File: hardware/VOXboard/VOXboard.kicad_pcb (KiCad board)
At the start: 2 copper layers, 52 parts, among them J1 USB-C 2.0 16P, J8 8P8C_LED_Shielded_x4, Q1 2N7002, U1 OPA333, U3 OPA333, U4 STM32F411CEUx, U7 HT7533, Y1 12M

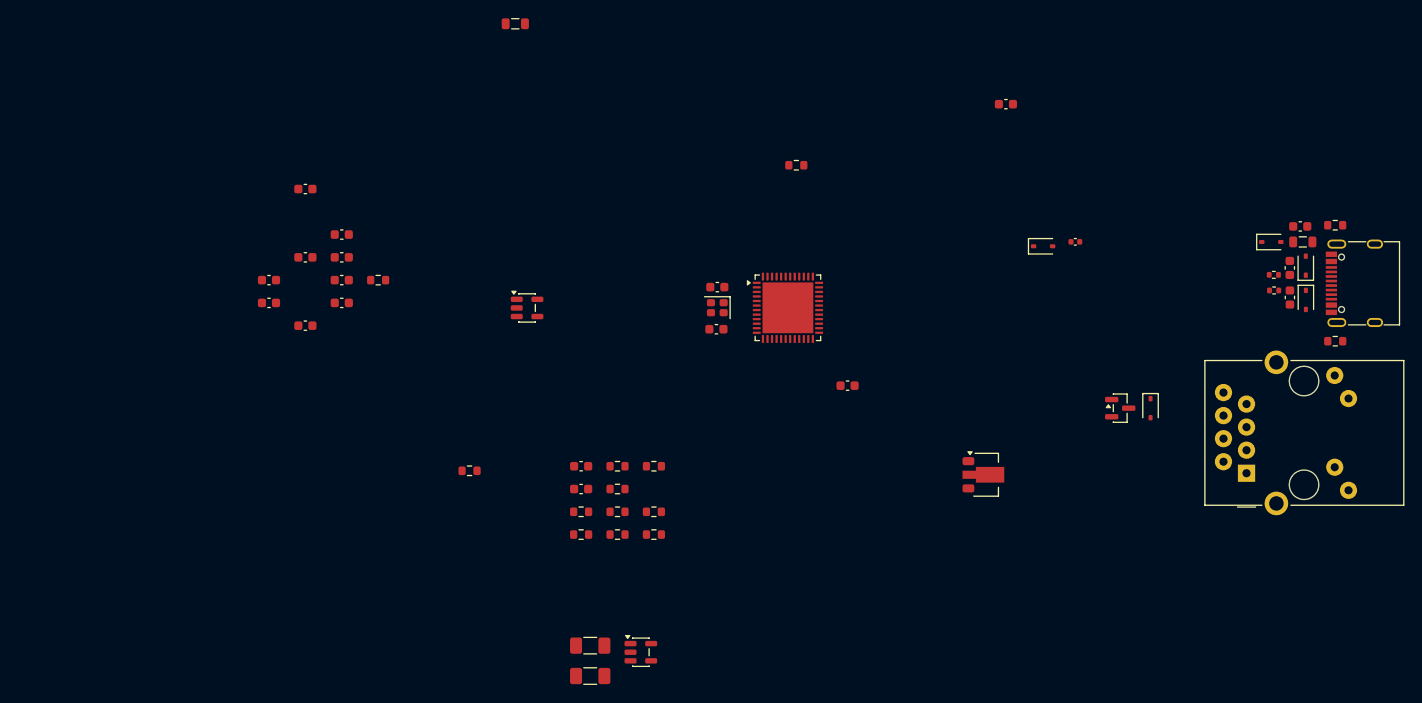
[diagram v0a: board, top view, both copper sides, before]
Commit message: Worked on OpAmp design in uSimmics.  Updated schematic.
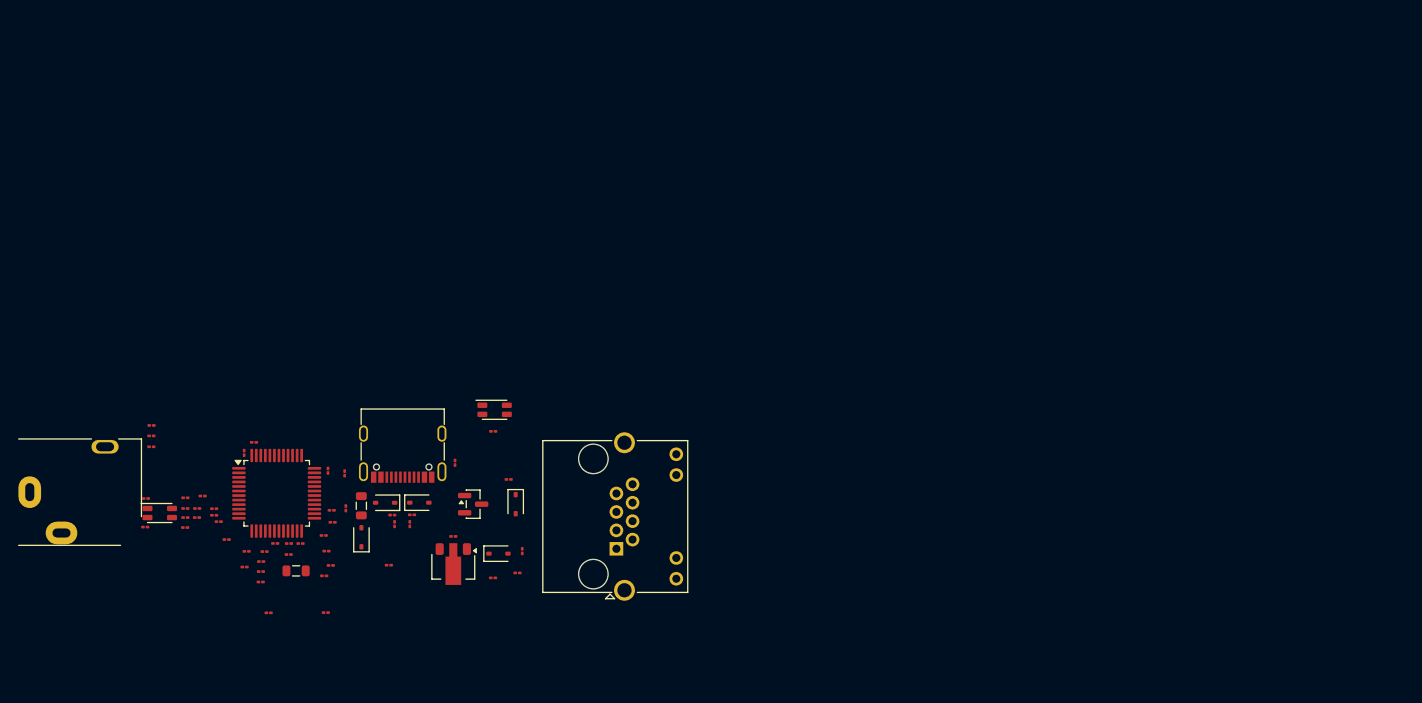
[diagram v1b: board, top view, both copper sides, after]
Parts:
- removed C20: 1n, Capacitor_SMD:C_1206_3216Metric_Pad1.33x1.80mm_HandSolder
- removed C5: 4.7u, Capacitor_SMD:C_0603_1608Metric
- removed R12: 1M, Resistor_SMD:R_0603_1608Metric
- removed R13: 20K, Resistor_SMD:R_0603_1608Metric
- removed U1, U3: OPA333, Package_TO_SOT_SMD:SOT-23-5
- removed U4: STM32F411CEUx, Package_DFN_QFN:QFN-48-1EP_7x7mm_P0.5mm_EP5.6x5.6mm
- removed Y1: 12M, Crystal:Crystal_SMD_2016-4Pin_2.0x1.6mm
- added C12: 470p, Capacitor_SMD:C_01005_0402Metric, F.Cu at (137.9, 99.2)
- added C19: 470p, Capacitor_SMD:C_01005_0402Metric, F.Cu at (142.3, 96.0)
- added C22: 470p, Capacitor_SMD:C_01005_0402Metric, F.Cu at (142.3, 99.2)
- added C23: 470p, Capacitor_SMD:C_01005_0402Metric, F.Cu at (138.6, 90.3)
- added C24: 1n, Capacitor_SMD:C_01005_0402Metric, F.Cu at (150.7, 104.1)
- added C25: 100n, Capacitor_SMD:C_01005_0402Metric, F.Cu at (157.6, 100.1)
- added C26: 1u, Capacitor_SMD:C_01005_0402Metric, F.Cu at (157.9, 101.8)
- added C27: 100n, Capacitor_SMD:C_01005_0402Metric, F.Cu at (158.5, 97.3)
- added C28: 4.7n, Capacitor_SMD:C_01005_0402Metric, F.Cu at (149.1, 101.8)
- added C29: 1n, Capacitor_SMD:C_01005_0402Metric, F.Cu at (157.8, 108.6)
- added FL1: APCW3216-222P2T, Inductor_SMD:L_CommonMode_Wurth_WE-CNSW-1206, F.Cu at (139.5, 97.6)
- added FL2: APCW3216-222P2T, Inductor_SMD:L_CommonMode_Wurth_WE-CNSW-1206, F.Cu at (176.4, 86.2)
- added J3: MicJack, Connector_Audio:Jack_3.5mm_CUI_SJ1-3513N_Horizontal, F.Cu at (125.2, 95.3)
- added R17: 0, Resistor_SMD:R_01005_0402Metric, F.Cu at (138.6, 88.0)
- added R18: 10K 0.1%, Resistor_SMD:R_01005_0402Metric, F.Cu at (145.5, 97.9)
- added R19: 10K 0.1%, Resistor_SMD:R_01005_0402Metric, F.Cu at (145.5, 97.2)
- added R20: 4k7, Resistor_SMD:R_01005_0402Metric, F.Cu at (146.9, 100.5)
- added R21: 10K 0.1%, Resistor_SMD:R_01005_0402Metric, F.Cu at (146.0, 98.6)
- added R22: 4k7, Resistor_SMD:R_01005_0402Metric, F.Cu at (158.4, 103.4)
- added R23: 27k, Resistor_SMD:R_01005_0402Metric, F.Cu at (148.9, 103.6)
- added R3: 2k2, Resistor_SMD:R_01005_0402Metric, F.Cu at (138.6, 89.1)
- added U2: STM32G474CBTx, Package_QFP:LQFP-48_7x7mm_P0.5mm, F.Cu at (152.4, 95.5)
- C1, C11, C14, C16, C17, C18, C2, C3, C33, C34, C6, C8: footprint Capacitor_SMD:C_0603_1608Metric -> Capacitor_SMD:C_01005_0402Metric
- C10: value 20p -> 470n film; footprint Capacitor_SMD:C_0603_1608Metric -> Capacitor_SMD:C_01005_0402Metric
- C13: value 20p -> 470p; footprint Capacitor_SMD:C_0603_1608Metric -> Capacitor_SMD:C_01005_0402Metric
- C15: value 2.2u -> 1u; footprint Capacitor_SMD:C_0603_1608Metric -> Capacitor_SMD:C_01005_0402Metric
- C21: footprint Capacitor_SMD:C_0402_1005Metric -> Capacitor_SMD:C_01005_0402Metric
- C4: value 33p -> 100p; footprint Capacitor_SMD:C_0603_1608Metric -> Capacitor_SMD:C_01005_0402Metric
- C7: value 1n -> 470n film; footprint Capacitor_SMD:C_0603_1608Metric -> Capacitor_SMD:C_01005_0402Metric
- C9: value 1u -> 100p; footprint Capacitor_SMD:C_1206_3216Metric_Pad1.33x1.80mm_HandSolder -> Capacitor_SMD:C_01005_0402Metric
- J8: value 8P8C_LED_Shielded_x4 -> RJ45_LED; footprint Connector_RJ:RJ45_Amphenol_RJMG1BD3B8K1ANR -> Connector_RJ:RJ45_Amphenol_RJHSE538X
- R1, R16, R2, R26, R8: footprint Resistor_SMD:R_0603_1608Metric -> Resistor_SMD:R_01005_0402Metric
- R10: value 100K -> 220; footprint Resistor_SMD:R_0603_1608Metric -> Resistor_SMD:R_01005_0402Metric
- R11: value 1K5 -> 2K2; footprint Resistor_SMD:R_0603_1608Metric -> Resistor_SMD:R_01005_0402Metric
- R14: value 1M -> 13k; footprint Resistor_SMD:R_0603_1608Metric -> Resistor_SMD:R_01005_0402Metric
- R15: value 20K -> 13k; footprint Resistor_SMD:R_0603_1608Metric -> Resistor_SMD:R_01005_0402Metric
- R4: value 51K -> 47; footprint Resistor_SMD:R_0603_1608Metric -> Resistor_SMD:R_01005_0402Metric
- R5, R6: footprint Resistor_SMD:R_0402_1005Metric -> Resistor_SMD:R_01005_0402Metric
- R7: value 150K -> 10K; footprint Resistor_SMD:R_0603_1608Metric -> Resistor_SMD:R_01005_0402Metric
- R9: value 510K -> 220; footprint Resistor_SMD:R_0603_1608Metric -> Resistor_SMD:R_01005_0402Metric
- moved R2 112.5 mm to (159.9, 93.3), turned to 90 degrees
- moved C2 109.7 mm to (160.0, 97.1), turned to 90 degrees
- moved FB1 107.7 mm to (161.7, 96.8), turned to -90 degrees
- moved J1 107.5 mm to (166.3, 90.0), turned to 180 degrees
- moved D5 105.4 mm to (161.8, 100.3), turned to 90 degrees
- moved D1 104.8 mm to (164.4, 96.5), turned to 180 degrees
- moved C3 102.6 mm to (165.2, 97.8), turned to 180 degrees
- moved R6 100.7 mm to (165.4, 98.8), turned to 90 degrees
- moved D2 100.2 mm to (168.1, 96.5), turned to 0 degrees
- moved C1 99.7 mm to (167.3, 97.8), turned to 0 degrees
- moved R5 98.7 mm to (167.1, 98.8), turned to 90 degrees
- moved R1 97.9 mm to (172.1, 92.1), turned to 90 degrees
- moved C16 92.3 mm to (148.8, 91.0), turned to 90 degrees
- moved R8 74.8 mm to (150.7, 105.2)
- moved Q1 72.1 mm to (174.1, 96.7)
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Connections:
- C10 pad 1: Net-(U4-PH0) -> Net-(C10-Pad1)
- C10 pad 2: GND -> /MIC_N_AC
- C11 pad 1: /+3V3 -> /VDD
- C13 pad 1: Net-(U4-PH1) -> /MIC_P
- C14 pad 1: /+3V3 -> /VDD
- C15 pad 1: Net-(U4-VCAP1) -> Net-(U2-VREF+)
- C16 pad 1: /+3V3 -> /VDD
- C17 pad 1: /AVCC -> /VDDA
- C18 pad 1: /AVCC -> /VDDA
- C33 pad 1: /+3V3 -> /VDD
- C34 pad 1: /+3V3 -> /VDD
- C4 pad 1: Net-(U1--) -> /MIC_P_TX
- C4 pad 2: /MIC_ADC -> GND
- C6 pad 1: Net-(U4-NRST) -> Net-(U2-VREF+)
- C7 pad 1: Net-(C7-Pad1) -> Net-(C22-Pad1)
- C7 pad 2: Net-(U1-+) -> /MIC_P_AC
- C8 pad 1: /+3V3 -> /VDD
- C9 pad 1: /+3v3 -> /MIC_N_TX
- FB2 pad 2: /AVCC -> /VDDA
- R10 pad 1: Net-(U3--) -> Net-(FL1-Pad2)
- R10 pad 2: Net-(R10-Pad2) -> Net-(C10-Pad1)
- R11 pad 2: /+3v3 -> /8V
- R14 pad 1: GND -> Net-(C29-Pad1)
- R14 pad 2: Net-(U1-+) -> /VINP3
- R15 pad 1: GND -> /VOUT1
- R15 pad 2: Net-(U3--) -> Net-(C29-Pad1)
- R4 pad 1: Net-(R10-Pad2) -> /VMID
- R4 pad 2: Net-(C20-Pad1) -> /VOUT4
- R7 pad 1: Net-(C20-Pad1) -> Net-(U2-PB13)
- R7 pad 2: Net-(U1--) -> /VDDA
- R8 pad 2: Net-(U4-BOOT0) -> Net-(U2-PB13)
- R9 pad 1: Net-(C20-Pad1) -> Net-(FL1-Pad3)
- R9 pad 2: /MIC_ADC -> Net-(C22-Pad1)
